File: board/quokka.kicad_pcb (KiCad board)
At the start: 4 copper layers, 228.6 x 184.1 mm, 337 parts, among them J1301 FPGA JTAG, J201 Barrel_Jack, J301 ARM SWD, J302 Conn_01x02, J303 Conn_01x09, J304 Conn_01x03, J305 USB_B, J401 Conn_01x09, Q1201 Q_NPN_BEC, Q1301 Q_NPN_BEC, Q1401 Q_NPN_BEC, Q1402 Q_NPN_BEC, Q1403 Q_NPN_BEC, Q201 Q_PMOS_GSD, Q601 Q_PMOS_GSD, Q602 Q_PMOS_GSD, Q603 Q_PMOS_GSD, Q604 Q_PMOS_GSD, Q605 Q_PMOS_GSD, Q606 Q_PMOS_GSD, Q607 Q_PMOS_GSD, Q608 Q_PMOS_GSD, Q701 Q_PMOS_GSD, Q702 Q_PMOS_GSD, Q703 Q_PMOS_GSD, Q704 Q_PMOS_GSD, Q705 Q_PMOS_GSD, Q706 Q_PMOS_GSD, Q707 Q_PMOS_GSD, Q708 Q_PMOS_GSD, Q801 Q_PMOS_GSD, Q802 Q_PMOS_GSD, Q803 Q_PMOS_GSD, Q804 Q_PMOS_GSD, Q805 Q_PMOS_GSD, Q806 Q_PMOS_GSD, Q807 Q_PMOS_GSD, SW901 SW_SPST, SW902 SW_SPST, SW903 SW_SPST, SW904 SW_SPST, SW905 SW_SPST, SW906 SW_SPST, SW907 SW_SPST, SW908 SW_SPST, SW909 SW_SPST, SW910 SW_SPST, SW911 SW_SPST, SW912 SW_SPST, SW913 SW_SPST, SW914 SW_SPST, SW915 SW_SPST, SW916 SW_SPST, SW917 SW_SPST, SW918 SW_SPST, SW919 SW_SPST, SW920 SW_SPST, SW921 SW_SPST, SW922 SW_SPST, SW923 SW_SPST, SW924 SW_SPST, SW925 SW_SPST, SW926 SW_SPST, SW927 SW_SPST, SW928 SW_SPST, SW929 SW_SPST, SW930 SW_SPST, U1001 DIN96, U1101 AS6C8008, U1201 74HCT245, U1202 6502, U1203 74HCT245, U1204 74HCT245, U1205 74HCT245, U1401 74LVC4245A, U1402 74LVC4245A, U1403 74LVC4245A, U1404 74LVC4245A, U1405 74LVC4245A, U1406 74LVC4245A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

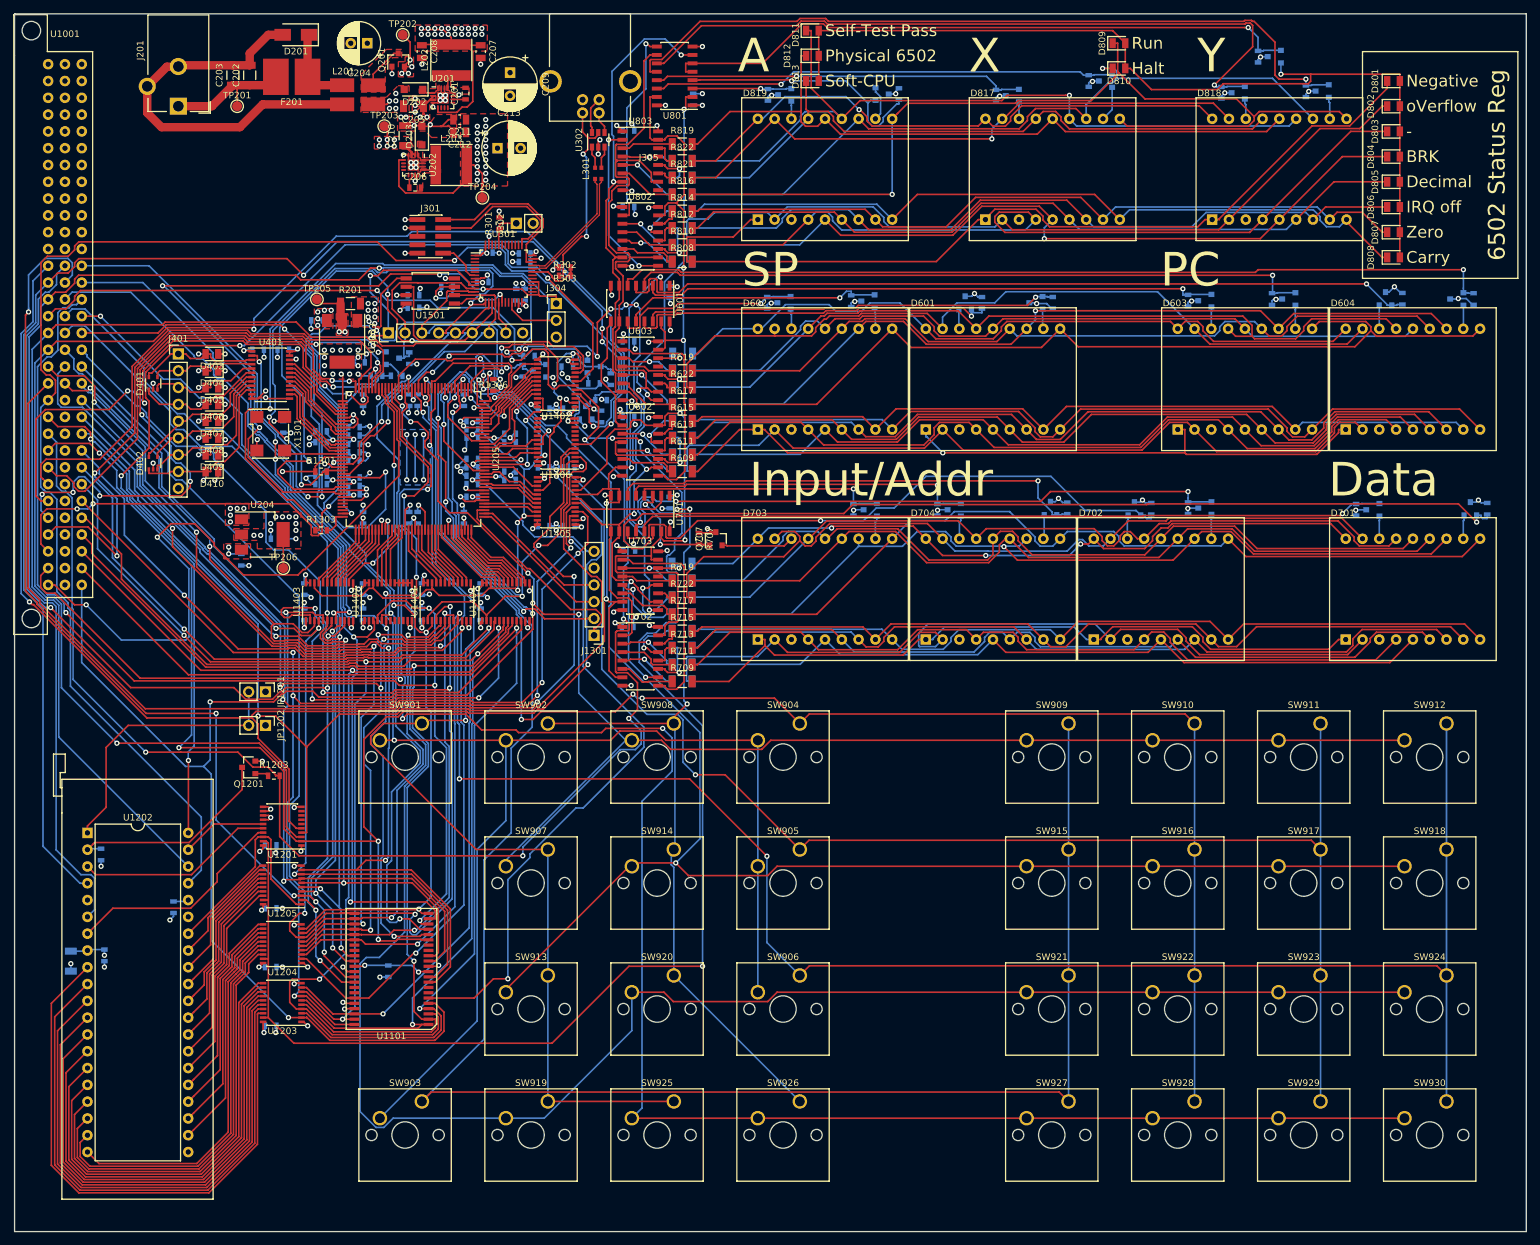
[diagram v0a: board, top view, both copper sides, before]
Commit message: Cleaned up silkscreen designators
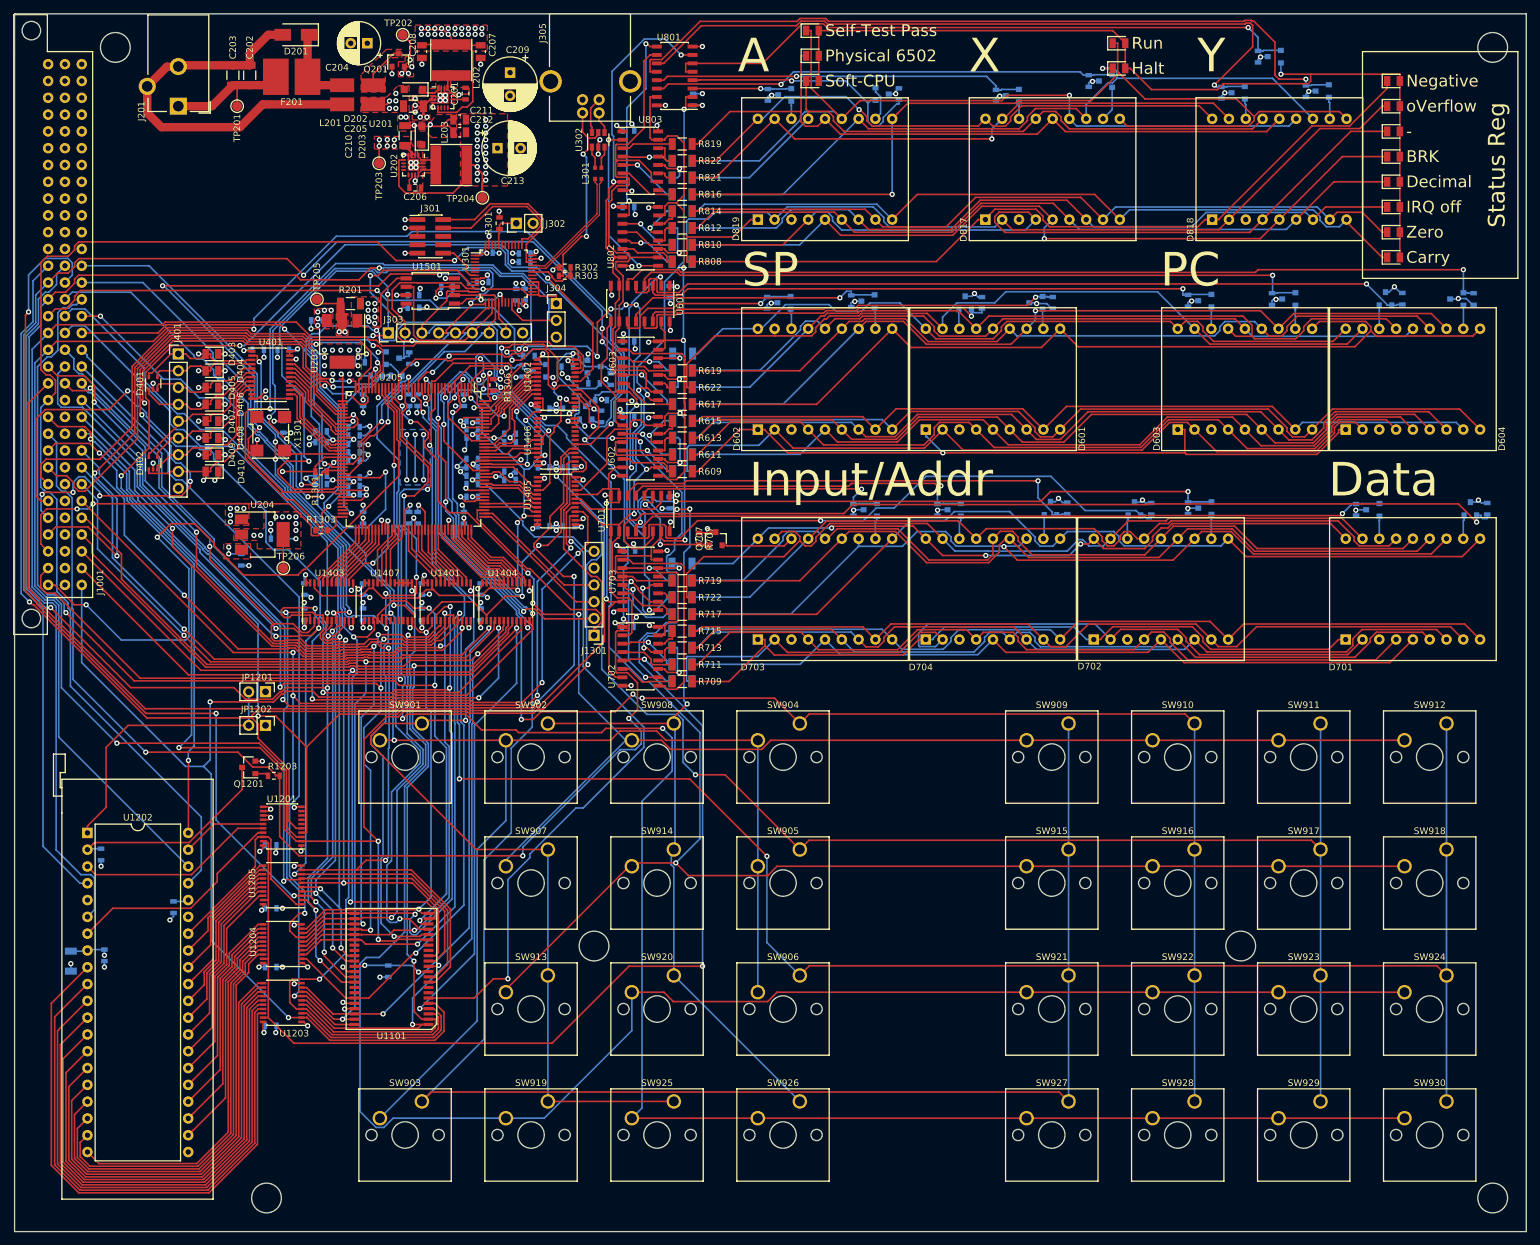
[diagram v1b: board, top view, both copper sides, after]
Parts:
- added MK101: Mounting_Hole, MountingHole:MountingHole_4.5mm, F.Cu at (175.9, 40.0)
- added MK102: Mounting_Hole, MountingHole:MountingHole_4.5mm, F.Cu at (384.2, 40.0)
- added MK103: Mounting_Hole, MountingHole:MountingHole_4.5mm, F.Cu at (384.2, 214.0)
- added MK104: Mounting_Hole, MountingHole:MountingHole_4.5mm, F.Cu at (346.1, 175.9)
- added MK105: Mounting_Hole, MountingHole:MountingHole_4.5mm, F.Cu at (248.3, 175.9)
- added MK106: Mounting_Hole, MountingHole:MountingHole_4.5mm, F.Cu at (198.8, 214.0)
- moved TP203 5.67 mm to (215.8, 57.5)
- renumbered U1001 to J1001
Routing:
- net Net-(Q703-Pad1): track 38.5 -> 39.9 mm
- net GND: vias 189 -> 190
- net +1V2: vias 14 -> 13
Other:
- board text added: "Status Reg"
- board text removed: "6502 Status Reg"

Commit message: Added fids, made PDF
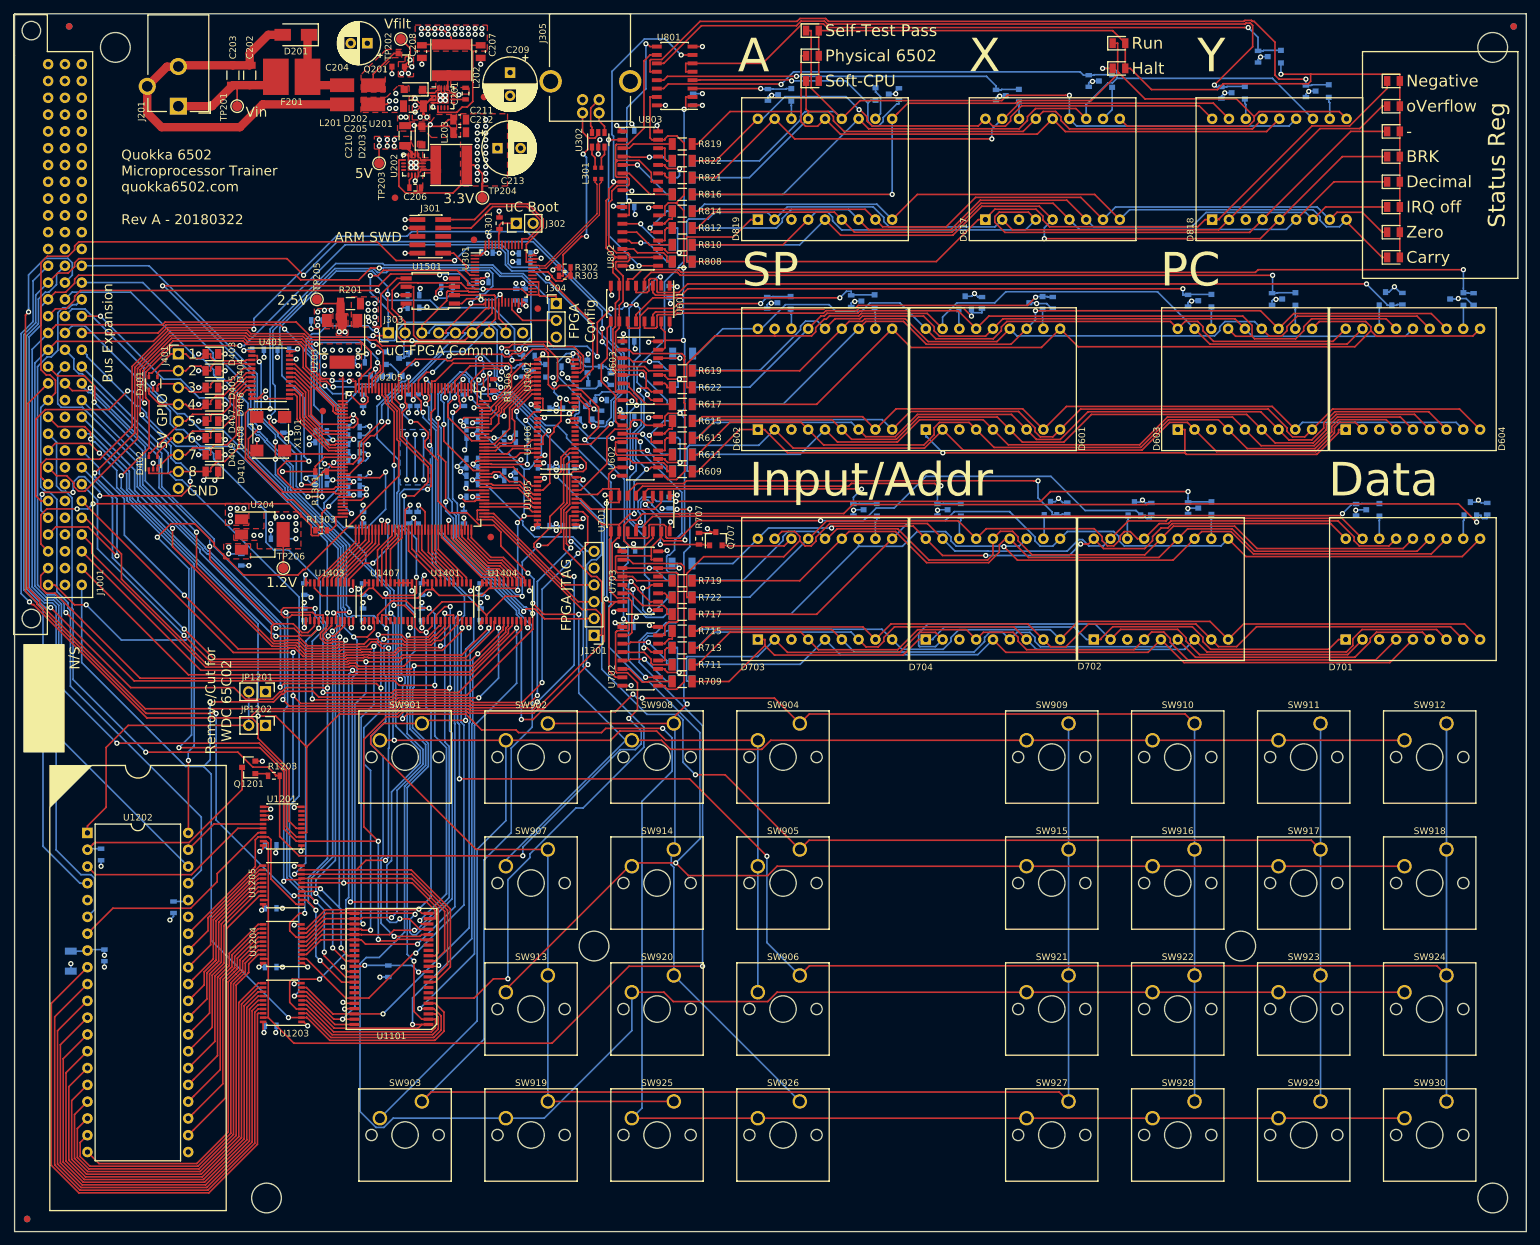
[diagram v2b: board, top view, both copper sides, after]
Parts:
- added FID101: Fiducial, Fiducial:Fiducial_1mm_Dia_2.54mm_Outer_CopperTop, F.Cu at (162.6, 217.2)
- added FID102: Fiducial, Fiducial:Fiducial_1mm_Dia_2.54mm_Outer_CopperTop, F.Cu at (168.9, 36.8)
- added FID103: Fiducial, Fiducial:Fiducial_1mm_Dia_2.54mm_Outer_CopperTop, F.Cu at (387.4, 36.8)
- added FID104: Fiducial, Fiducial:Fiducial_1mm_Dia_2.54mm_Outer_CopperBottom, F.Cu at (162.6, 217.2)
- added FID105: Fiducial, Fiducial:Fiducial_1mm_Dia_2.54mm_Outer_CopperBottom, F.Cu at (168.9, 36.8)
- added FID106: Fiducial, Fiducial:Fiducial_1mm_Dia_2.54mm_Outer_CopperBottom, F.Cu at (387.4, 36.8)
- added FID107: Fiducial, Fiducial:Fiducial_1mm_Dia_2.54mm_Outer_CopperTop, F.Cu at (207.3, 95.0)
- added FID108: Fiducial, Fiducial:Fiducial_1mm_Dia_2.54mm_Outer_CopperTop, F.Cu at (232.7, 114.0)
- added FID109: Fiducial, Fiducial:Fiducial_1mm_Dia_2.54mm_Outer_CopperTop, F.Cu at (231.6, 47.5)
- added FID110: Fiducial, Fiducial:Fiducial_1mm_Dia_2.54mm_Outer_CopperTop, F.Cu at (218.2, 62.7)
- added FID111: Fiducial, Fiducial:Fiducial_1mm_Dia_2.54mm_Outer_CopperTop, F.Cu at (230.1, 69.1)
- added FID112: Fiducial, Fiducial:Fiducial_1mm_Dia_2.54mm_Outer_CopperTop, F.Cu at (239.8, 79.5)
- moved TP202 0.69 mm to (219.1, 38.7)
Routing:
- net /FPGA/G2: track 12.1 -> 13.5 mm
- net /FPGA/R3: track 219.0 -> 220.2 mm
- net /FPGA/G3: track 12.5 -> 13.6 mm
- net /FPGA/G4: track 12.4 -> 13.5 mm
- net Net-(C204-Pad1): track 22.6 -> 22.1 mm
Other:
- board text added: "1"
- board text added: "1.2V"
- board text added: "2"
- board text added: "2.5V"
- board text added: "3"
- board text added: "3.3V"
- board text added: "4"
- board text added: "5"
- board text added: "5V"
- board text added: "5V GPIO"
- board text added: "6"
- board text added: "7"
- board text added: "8"
- board text added: "ARM SWD"
- board text added: "Bus Expansion"
- board text added: "FPGA Config"
- board text added: "FPGA JTAG"
- board text added: "GND"
- board text added: "Quokka 6502 Microprocessor Trainer quokka6502.com"
- board text added: "Remove/Cut for WDC 65C02"
- board text added: "Rev A - 20180322"
- board text added: "S/N"
- board text added: "Vfilt"
- board text added: "Vin"
- board text added: "uC Boot"
- board text added: "uC-FPGA Comm"

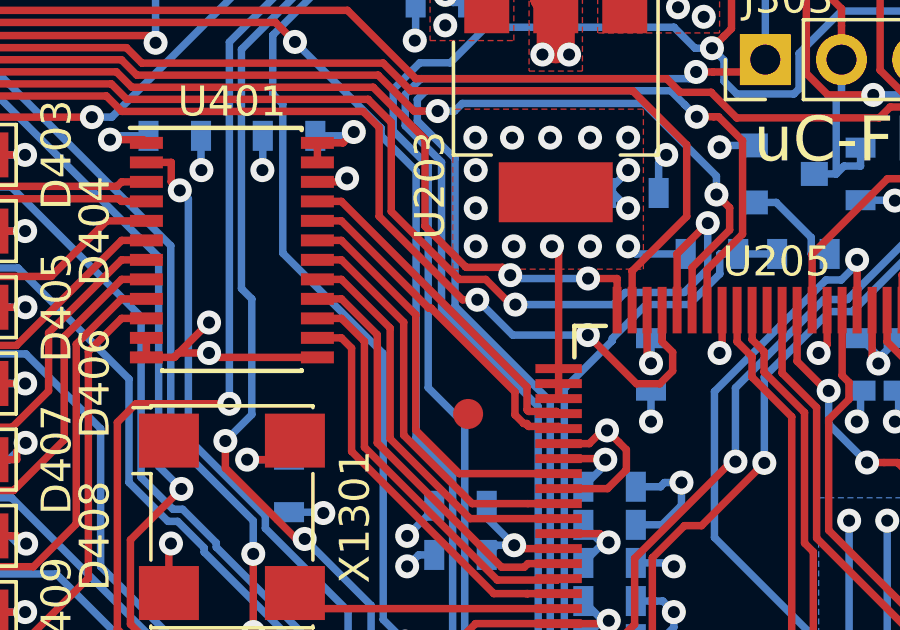
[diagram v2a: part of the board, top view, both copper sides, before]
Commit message: Resolved accidental DRC error
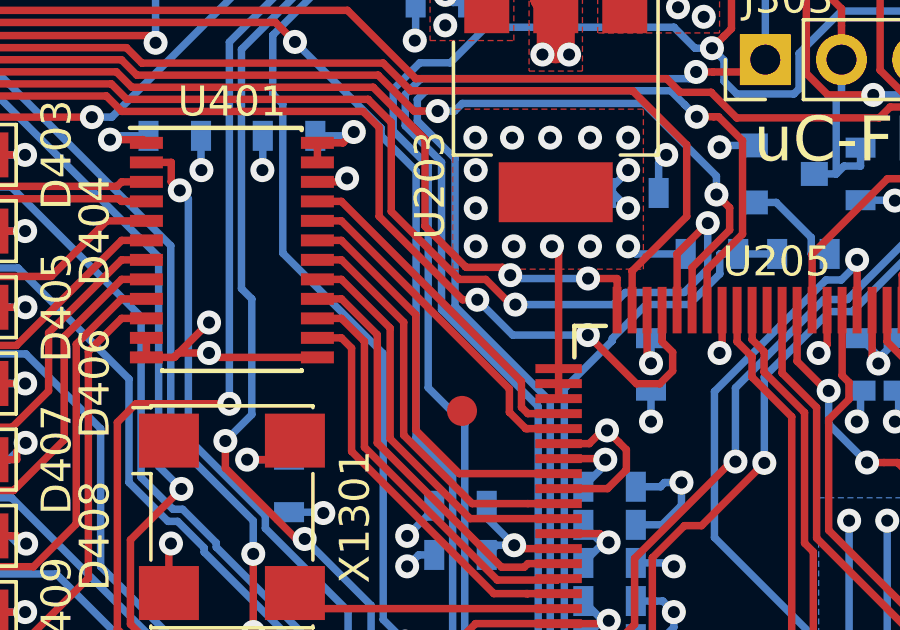
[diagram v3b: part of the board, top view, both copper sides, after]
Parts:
- moved FID107 0.23 mm to (207.1, 94.9)
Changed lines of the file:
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@@
     (thickness 1.6)
     (drawings 66)
-    (tracks 6962)
+    (tracks 6956)
     (zones 0)
     (modules 355)
@@
   )
   (module Fiducial:Fiducial_1mm_Dia_2.54mm_Outer_CopperTop (layer F.Cu)
-    (at 207.264 94.996)
+    (at 207.0608 94.8944)
     (descr "Circular Fiducial, 1mm bare copper top; 2.54mm keepout")
     (tags marker)
@@
   (segment (start 205.519 91.6894) (end 203.04 89.21) (width 0.25) (layer F.Cu) (net 262))
   (segment (start 203.04 89.21) (end 202.24 89.21) (width 0.25) (layer F.Cu) (net 262))
-  (segment (start 206.028108 91.4672) (end 208.825189 94.264281) (width 0.25) (layer F.Cu) (net 263))
-  (segment (start 208.825189 94.264281) (end 208.825189 95.023603) (width 0.25) (layer F.Cu) (net 263))
-  (segment (start 209.227599 95.31481) (end 209.227599 95.356921) (width 0.25) (layer F.Cu) (net 263))
   (segment (start 202.24 88.56) (end 203.04 88.56) (width 0.25) (layer F.Cu) (net 263))
-  (segment (start 203.04 88.56) (end 205.947 91.4672) (width 0.25) (layer F.Cu) (net 263))
-  (segment (start 210.28 95.412401) (end 210.28 95.485) (width 0.25) (layer F.Cu) (net 263))
-  (segment (start 208.825189 95.023603) (end 209.116396 95.31481) (width 0.25) (layer F.Cu) (net 263))
-  (segment (start 205.947 91.4672) (end 206.028108 91.4672) (width 0.25) (layer F.Cu) (net 263))
-  (segment (start 209.116396 95.31481) (end 209.227599 95.31481) (width 0.25) (layer F.Cu) (net 263))
-  (segment (start 209.227599 95.356921) (end 209.283079 95.412401) (width 0.25) (layer F.Cu) (net 263))
-  (segment (start 209.283079 95.412401) (end 210.28 95.412401) (width 0.25) (layer F.Cu) (net 263))
-  (segment (start 210.2074 94.9124) (end 209.283079 94.9124) (width 0.25) (layer F.Cu) (net 264))
-  (segment (start 210.28 94.985) (end 210.2074 94.9124) (width 0.25) (layer F.Cu) (net 264))
-  (segment (start 209.283079 94.9124) (end 209.227599 94.85692) (width 0.25) (layer F.Cu) (net 264))
-  (segment (start 209.227599 94.85692) (end 209.227599 94.097599) (width 0.25) (layer F.Cu) (net 264))
-  (segment (start 209.227599 94.097599) (end 203.04 87.91) (width 0.25) (layer F.Cu) (net 264))
+  (segment (start 203.04 88.56) (end 208.639589 94.159589) (width 0.25) (layer F.Cu) (net 263))
+  (segment (start 208.639589 94.159589) (end 208.639589 94.938684) (width 0.25) (layer F.Cu) (net 263))
+  (segment (start 208.639589 94.938684) (end 209.185905 95.485) (width 0.25) (layer F.Cu) (net 263))
+  (segment (start 209.255 95.485) (end 210.28 95.485) (width 0.25) (layer F.Cu) (net 263))
+  (segment (start 209.185905 95.485) (end 209.255 95.485) (width 0.25) (layer F.Cu) (net 263))
+  (segment (start 209.042 94.772) (end 209.042 93.912) (width 0.25) (layer F.Cu) (net 264))
+  (segment (start 209.255 94.985) (end 209.042 94.772) (width 0.25) (layer F.Cu) (net 264))
+  (segment (start 210.28 94.985) (end 209.255 94.985) (width 0.25) (layer F.Cu) (net 264))
+  (segment (start 209.042 93.912) (end 203.04 87.91) (width 0.25) (layer F.Cu) (net 264))
   (segment (start 203.04 87.91) (end 202.24 87.91) (width 0.25) (layer F.Cu) (net 264))
   (segment (start 202.01 101.485) (end 201.49 100.965) (width 0.25) (layer F.Cu) (net 265))
